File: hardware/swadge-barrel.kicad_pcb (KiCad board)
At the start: 2 copper layers, 70.4 x 89.6 mm, 42 parts, among them J1 USB_B_Micro, SW1 4-1437565-2, SW2 4-1437565-2, SW3 4-1437565-2, SW4 SW_SPDT, U1 ESP-13-WROOM-02D, U2 DISP_OLED_UG-2864HSWEG01, U3 BUS_PCIexpress, U4 QMA6981, U5 AP1117-33

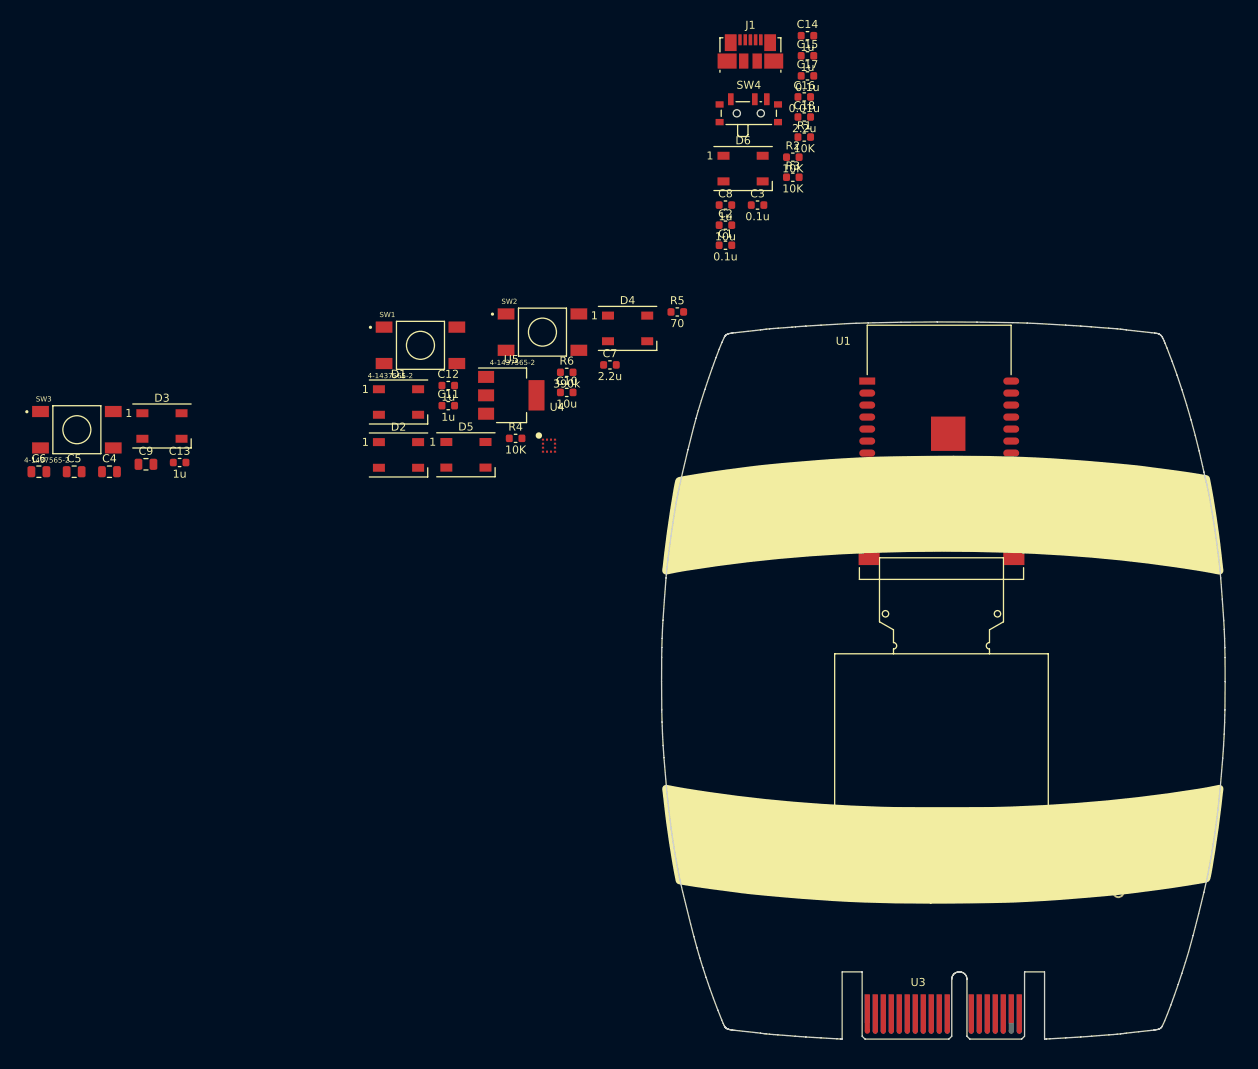
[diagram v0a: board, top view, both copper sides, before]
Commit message: Rough placement of barrel parts
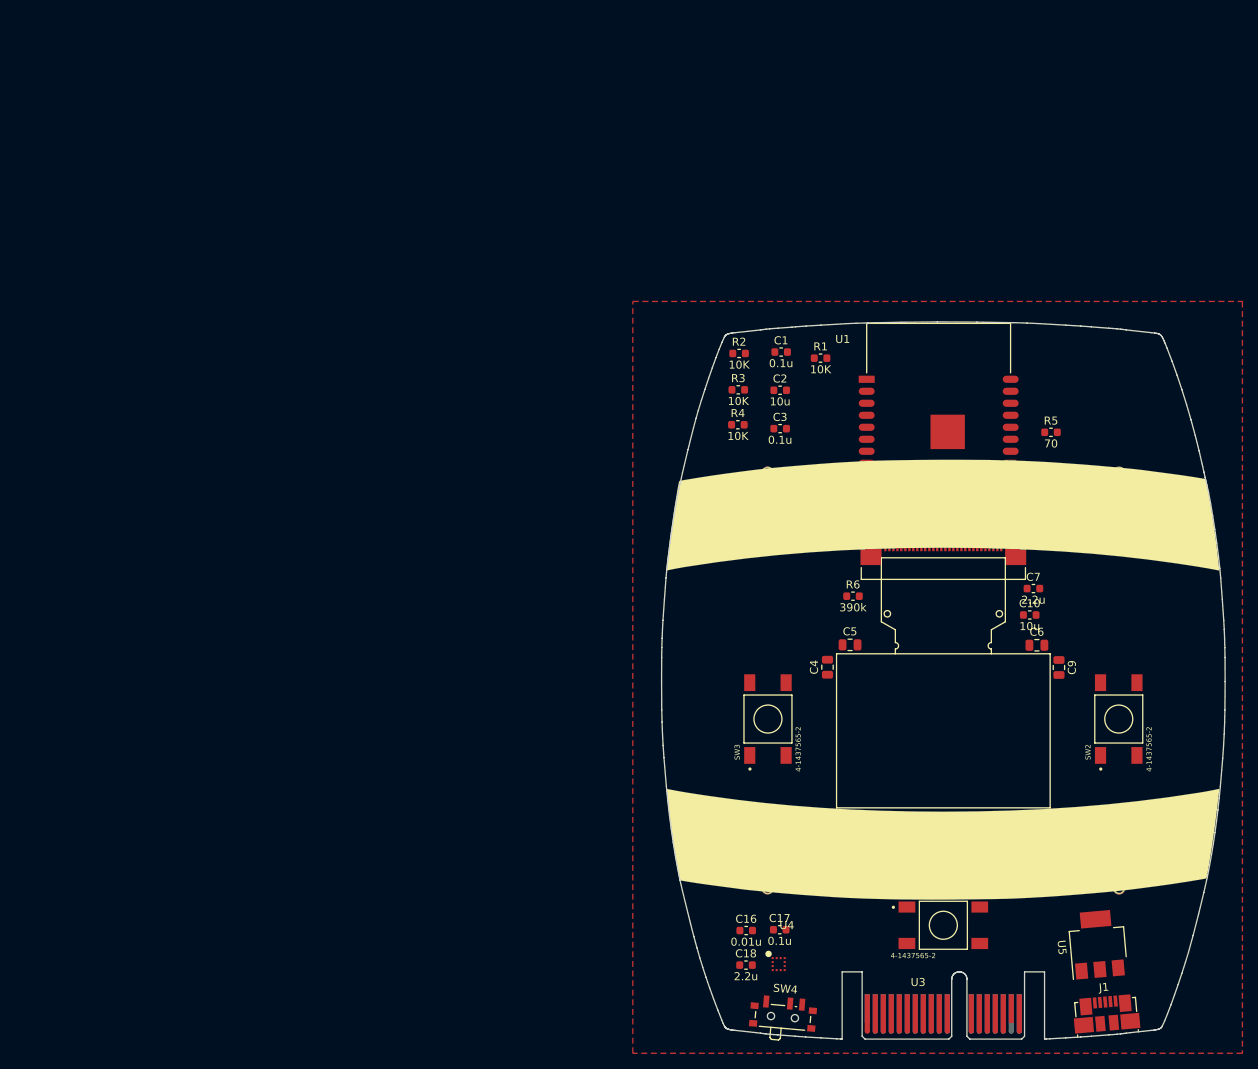
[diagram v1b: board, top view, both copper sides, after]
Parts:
- moved C13 131.9 mm to (173.2, 118.2), turned to 90 degrees
- moved J1 128.2 mm to (165.9, 139.8), turned to 5 degrees
- moved C6 126.6 mm to (157.2, 93.8)
- moved D3 120.1 mm to (167.4, 76.9), turned to 355 degrees
- moved C9 116.9 mm to (159.9, 96.6), turned to 270 degrees
- moved SW4 113.1 mm to (125.5, 139.9), turned to 355 degrees
- moved C17 106.8 mm to (125.0, 129.3)
- moved C18 106.3 mm to (120.8, 133.8)
- moved C14 104.9 mm to (151.5, 120.0), turned to 90 degrees
- moved C16 104.5 mm to (120.9, 129.4)
- moved U5 100.4 mm to (164.8, 131.2), turned to 95 degrees
- moved C15 99.6 mm to (117.3, 119.0), turned to 270 degrees
- moved C5 99.4 mm to (133.8, 93.7)
- moved SW1 97.6 mm to (145.5, 128.8)
- moved SW3 93.7 mm to (123.6, 103.0), turned to 90 degrees
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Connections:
- D6 pad 2: Net-(D6-Pad2) -> (no net)
- J1 pad 2: Net-(J1-Pad2) -> (no net)
- J1 pad 3: Net-(J1-Pad3) -> (no net)
- J1 pad 4: Net-(J1-Pad4) -> (no net)
- U2 pad 7: Net-(U2-Pad7) -> (no net)
- U4 pad 10: Net-(U4-Pad10) -> (no net)
- U4 pad 11: Net-(U4-Pad11) -> (no net)
- U4 pad 5: Net-(U4-Pad5) -> (no net)
- U4 pad 6: Net-(U4-Pad6) -> (no net)
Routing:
- added copper zone on F.Cu, net GND

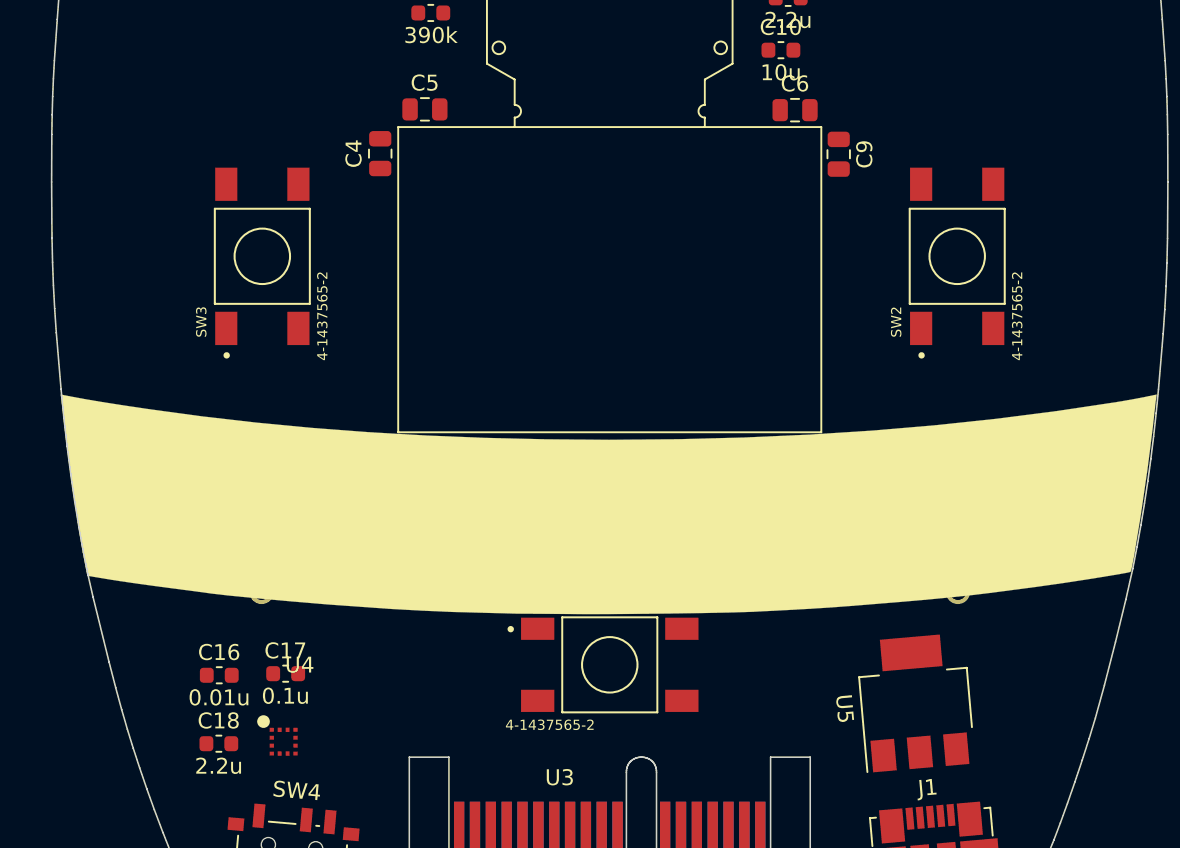
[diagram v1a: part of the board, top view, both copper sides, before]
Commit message: Added 12mm buttons
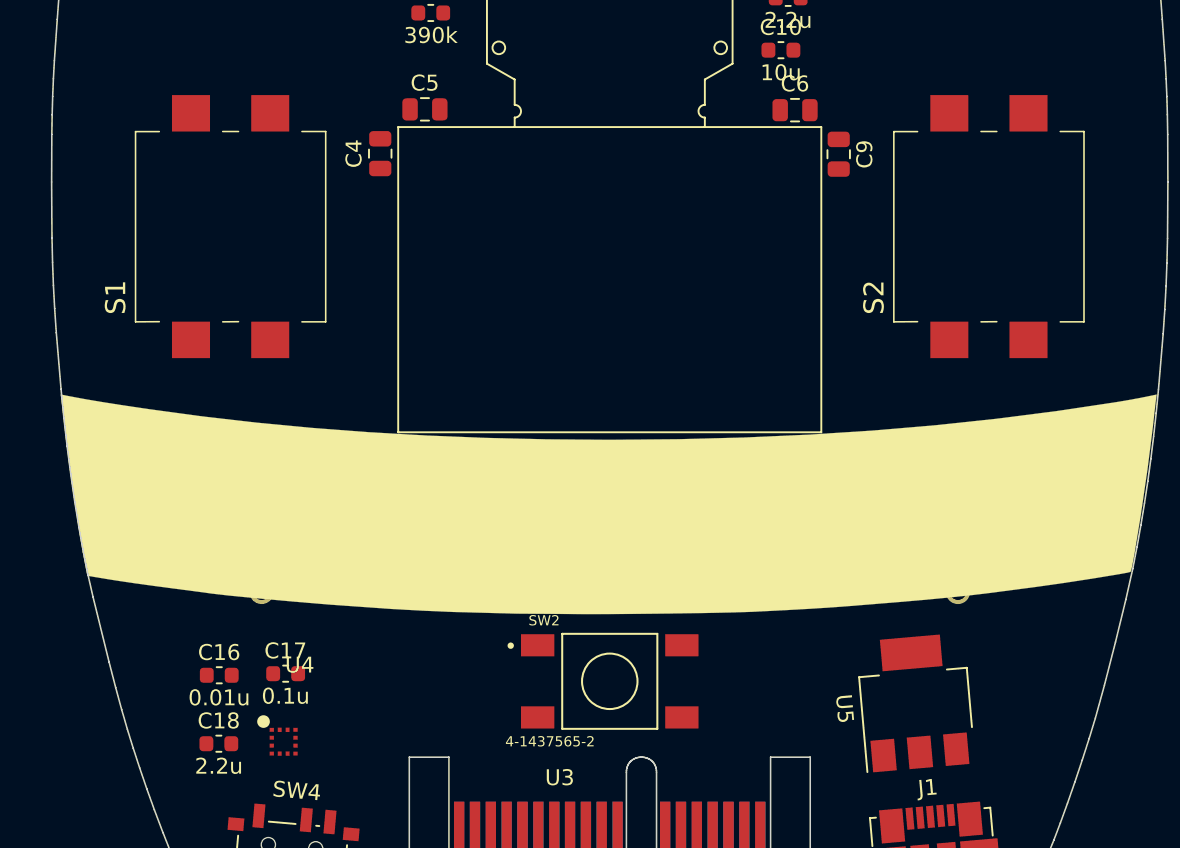
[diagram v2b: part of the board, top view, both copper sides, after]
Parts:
- removed SW1, SW3: 4-1437565-2, Swadge_Parts:SW_4-1437565-2
- added S1: B3FS-4002P, Swadge_Parts:B3FS4002P, F.Cu at (121.6, 100.0)
- added S2: B3FS-4002P, Swadge_Parts:B3FS4002P, F.Cu at (169.4, 100.0)
- moved SW2 34.6 mm to (145.5, 129.8), turned to 0 degrees

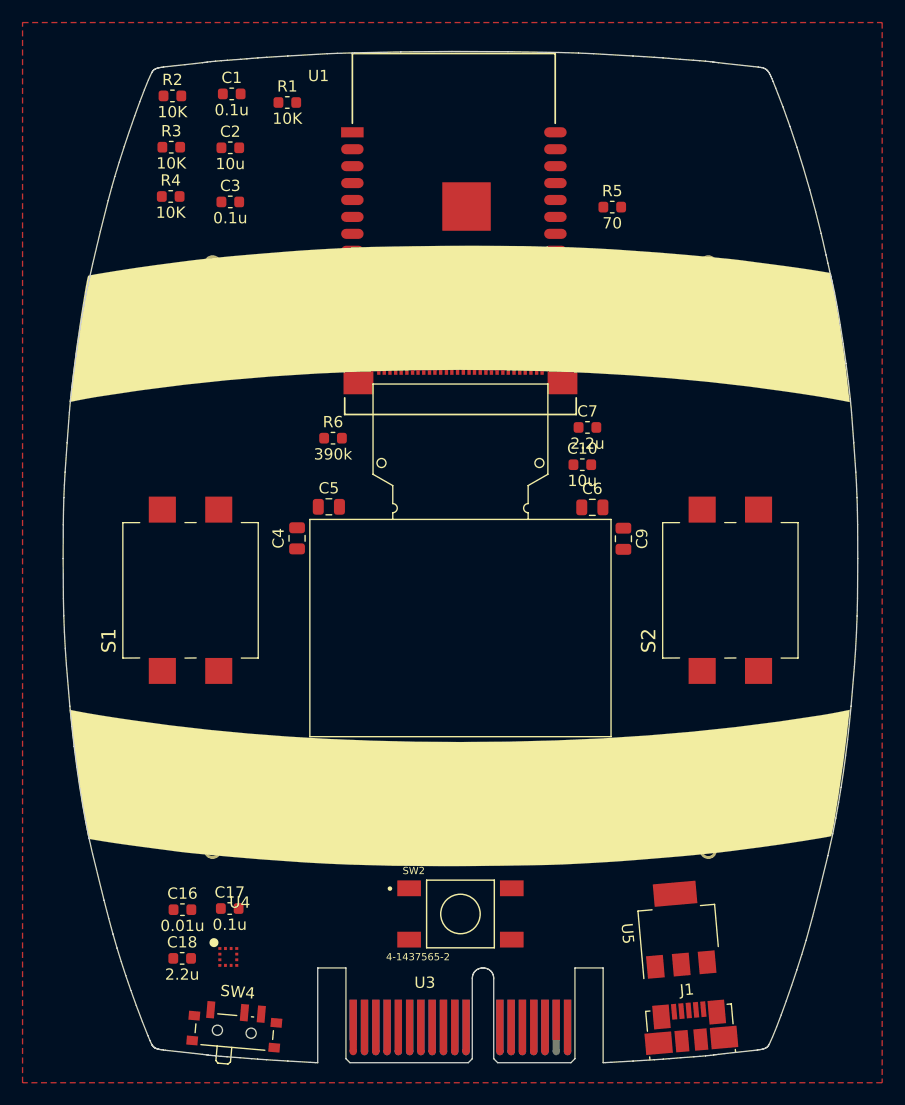
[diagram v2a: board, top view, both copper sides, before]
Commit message: More barrel layout, more barrel routing
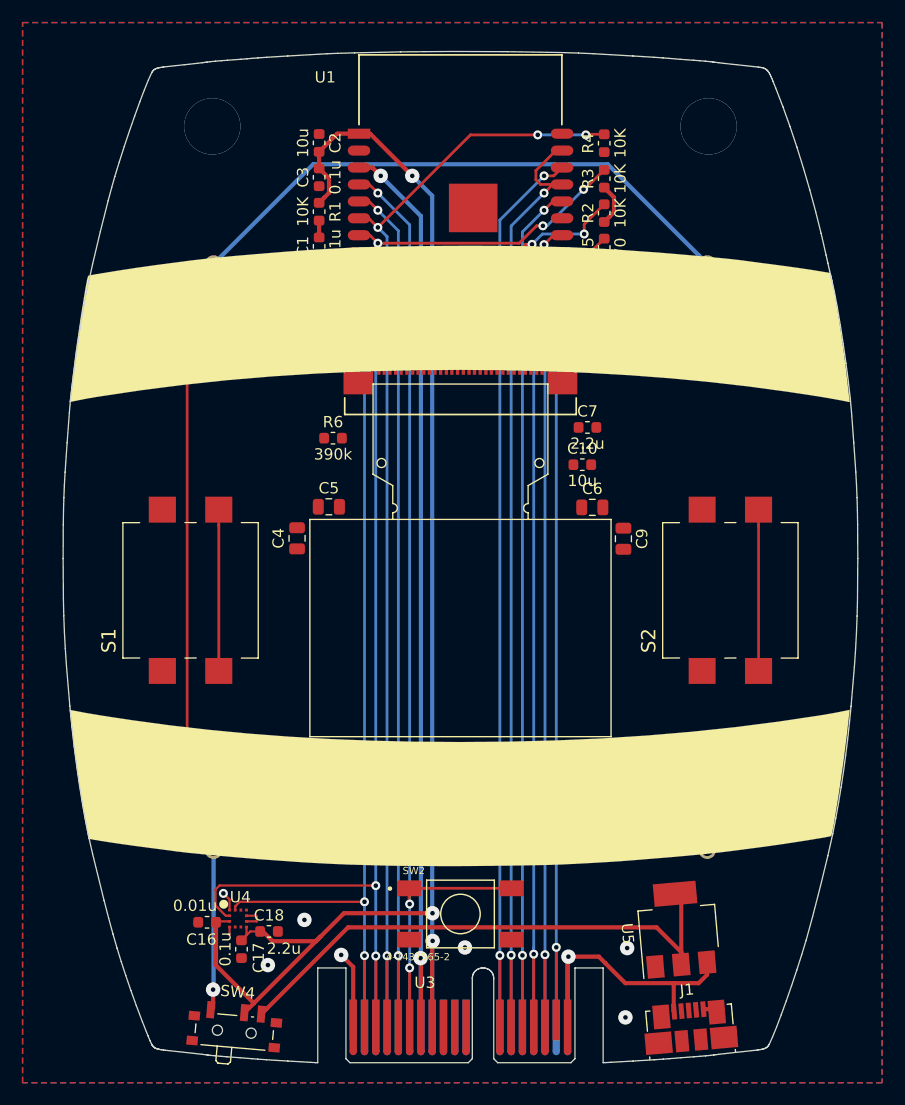
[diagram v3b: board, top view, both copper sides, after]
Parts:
- moved BT1 43.9 mm to (167.4, 98.2)
- moved BT2 43.9 mm to (123.6, 98.2)
- moved D1 43.9 mm to (167.4, 76.9), turned to 355 degrees
- moved D3 43.9 mm to (123.6, 76.9), turned to 5 degrees
- moved D4 43.9 mm to (123.6, 118.9), turned to 175 degrees
- moved D6 43.9 mm to (167.4, 118.9), turned to 185 degrees
- moved R2 39.7 mm to (158.2, 67.7), turned to 90 degrees
- moved R4 38.7 mm to (158.2, 61.5), turned to 90 degrees
- moved R3 38.5 mm to (158.2, 64.6), turned to 90 degrees
- moved C1 15.6 mm to (133.0, 70.6), turned to 90 degrees
- moved R1 10.1 mm to (133.0, 67.6), turned to 270 degrees
- moved C3 8.17 mm to (133.0, 64.5), turned to 90 degrees
- moved C18 8.06 mm to (128.5, 131.4)
- moved C2 7.89 mm to (133.0, 61.5), turned to 270 degrees
- moved C17 3.75 mm to (126.1, 132.9), turned to 270 degrees
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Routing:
- net +3V3: track 0.00 -> 237.9 mm, vias 0 -> 5
- net SDA: track 0.00 -> 117.7 mm, vias 0 -> 5
- net SCL: track 0.00 -> 112.8 mm, vias 0 -> 5
- net _RES: track 0.00 -> 102.8 mm, vias 0 -> 4
- net SW2: track 0.00 -> 95.5 mm, vias 0 -> 2
- net SW3: track 0.00 -> 92.6 mm, vias 0 -> 3
- net REST: track 0.00 -> 89.5 mm, vias 0 -> 2
- net SW4: track 0.00 -> 88.0 mm, vias 0 -> 2
- net ADC_PIN: track 0.00 -> 85.1 mm, vias 0 -> 2
- net AUD_PWR: track 0.00 -> 85.0 mm, vias 0 -> 2
- net SW5: track 0.00 -> 81.2 mm, vias 0 -> 2
- net RX: track 0.00 -> 80.1 mm, vias 0 -> 2
- net TX: track 0.00 -> 77.9 mm, vias 0 -> 2
- net Net-(BT1-Pad1): track 0.00 -> 51.1 mm
- net Net-(SW4-Pad3): track 0.00 -> 48.9 mm
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- added copper zone on B.Cu, net GND
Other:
- net class Power added: clearance 0.2, trace_width 0.375, via_dia 1.28, via_drill 0.4
- net class Thin added: clearance 0.2, trace_width 0.2, via_dia 0.8, via_drill 0.4

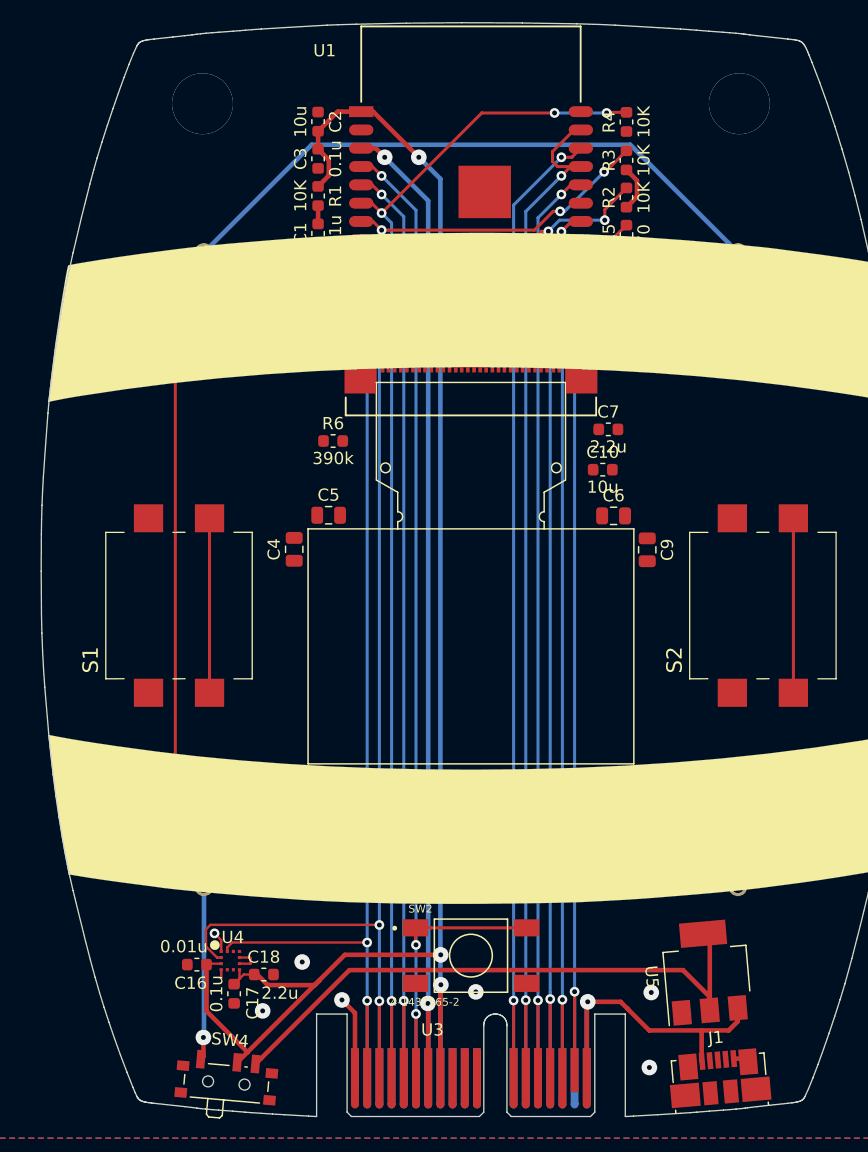
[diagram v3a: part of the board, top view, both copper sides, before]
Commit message: Added THT buzzer to barrel board
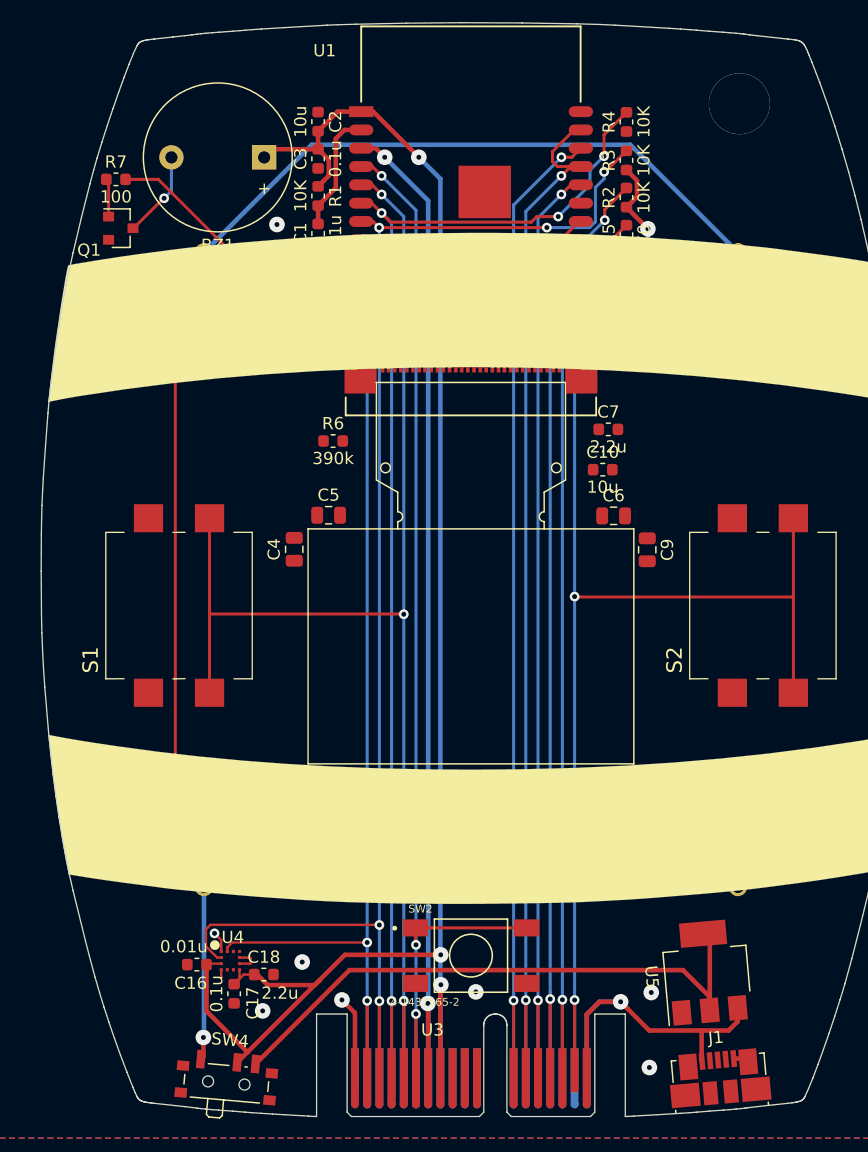
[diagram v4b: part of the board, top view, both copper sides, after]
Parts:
- added BZ1: Buzzer, Swadge_Parts:Buzzer_12x9.5RM7.6, F.Cu at (128.6, 64.4)
- added Q1: Q_NPN_BEC, Swadge_Parts:SOT-23, F.Cu at (116.8, 70.2)
- added R7: 100, Swadge_Parts:R_0603_1608Metric, F.Cu at (116.4, 66.2)
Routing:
- net SW5: track 81.2 -> 118.4 mm, vias 2 -> 3
- net SW4: track 88.0 -> 105.3 mm, vias 2 -> 3
- net SW2: track 95.5 -> 111.5 mm, vias 2 -> 3
- net +3V3: track 237.9 -> 250.7 mm, vias 5 -> 7
- net Net-(C1-Pad2): track 1.50 -> 9.97 mm
- net Net-(BZ1-Pad2): track 0.00 -> 7.16 mm, vias 0 -> 1
- net Net-(Q1-Pad1): track 0.00 -> 3.13 mm
- net _RES: track 102.8 -> 105.1 mm
- net SDA: track 117.7 -> 119.7 mm
- net +5V: track 29.5 -> 31.1 mm
- net GND: vias 8 -> 11
- net (no net): vias 2 -> 1
